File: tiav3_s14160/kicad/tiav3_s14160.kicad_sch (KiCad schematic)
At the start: 22 parts, among them J1 SSQ-103-01-G-D, J2 Conn_Coaxial, U1 OPA847IDBVT

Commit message: Tune tiav3 LPF values and export gerbers
Update LPF component values (560nH->330nH, 120pF->62pF) and tighten via diameter/drill DRC. Redirect plot/step outputs to ../manufacturing/ and commit the generated gerber set.
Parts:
- C2: value 120pF -> 62pF
- C3: value 120p -> 62pF
- L2: value 560nH -> 330nH
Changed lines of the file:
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@@
 			)
 		)
-		(property "Value" "560nH"
+		(property "Value" "330nH"
 			(at 233.553 109.271 0)
 			(effects
@@
 			)
 		)
-		(property "Value" "120pF"
+		(property "Value" "62pF"
 			(at 225.425 120.015 0)
 			(effects
@@
 			)
 		)
-		(property "Value" "120p"
+		(property "Value" "62pF"
 			(at 240.665 120.015 0)
 			(effects

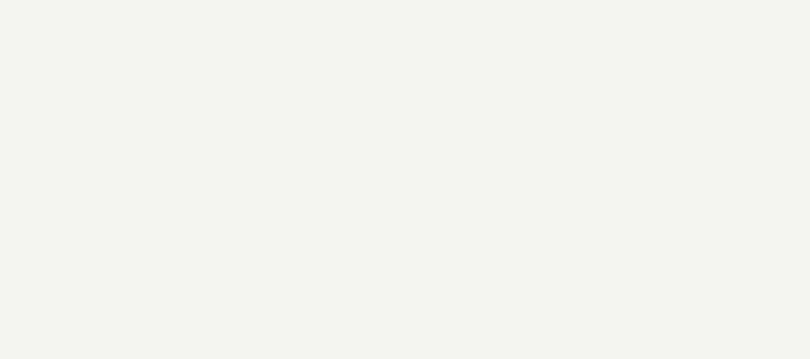
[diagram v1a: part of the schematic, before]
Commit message: Update KiCad designs for all 3 boards and re-export gerbers
- bias-control-lt8362: schematic + PCB updates, exported gerbers
  including new B_Paste/F_Paste layers
- power-supply: schematic + PCB updates, re-exported gerbers with new
  naming (.gbl/.gbs/.gto/.gtl/.gts) replacing old .gbr files, added
  paste layer exports
- tiav3_s14160: schematic + PCB updates, re-exported gerbers with new
  naming, added paste layer exports
- fp-lib-table updates across all four board projects
- new "w paste" gerber zip exports for assembly
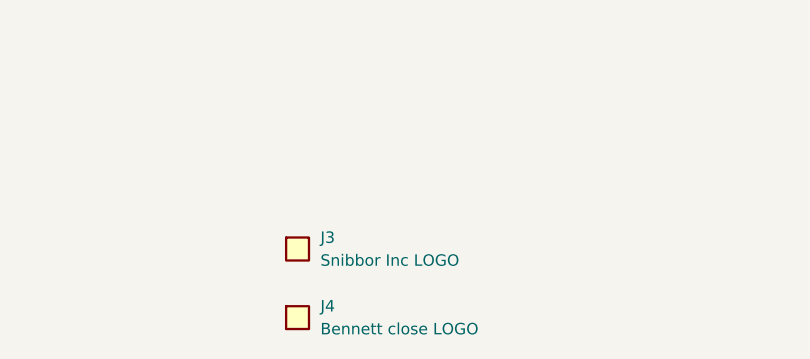
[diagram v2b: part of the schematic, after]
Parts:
- added J3: Snibbor Inc LOGO, snibbor_logos:snibbor_inc_logo, symbol Connector_Generic:Conn_01x01
- added J4: Bennett close LOGO, snibbor_logos:Bennett logo close 1 layered, symbol Connector_Generic:Conn_01x01
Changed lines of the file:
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@@
+	)
+	(symbol
+		(lib_id "Connector_Generic:Conn_01x01")
+		(at 49.53 172.72 0)
+		(unit 1)
+		(exclude_from_sim no)
+		(in_bom yes)
+		(on_board yes)
+		(dnp no)
+		(fields_autoplaced yes)
+		(property "Reference" "J4"
+			(at 52.07 171.4499 0)
+			(effects
+				(font
+					(size 1.27 1.27)
+				)
+				(justify left)
+			)
+		)
+		(property "Value" "Bennett close LOGO"
+			(at 52.07 173.9899 0)
+			(effects
+				(font
+					(size 1.27 1.27)
+				)
+				(justify left)
+			)
+		)
+		(property "Footprint" "snibbor_logos:Bennett logo close 1 layered"
+			(at 49.53 172.72 0)
+			(effects
+				(font
+					(size 1.27 1.27)
+				)
+				(hide yes)
+			)
+		)
+		(property "Datasheet" ""
+			(at 49.53 172.72 0)
+			(effects
+				(font
+					(size 1.27 1.27)
+				)
+				(hide yes)
+			)
+		)
+		(property "Description" ""
+			(at 49.53 172.72 0)
+			(effects
+				(font
+					(size 1.27 1.27)
+				)
+				(hide yes)
+			)
+		)
+		(instances
+			(project "tiav3_s14160"
+				(path "/548ba79d-aa60-452e-83bc-59e3672545ef"
+					(reference "J4")
+					(unit 1)
+				)
+			)
+		)
 	)
 	(symbol
@@
 					(unit 1)
 				)
+			)
+		)
+	)
+	(symbol
+		(lib_id "Connector_Generic:Conn_01x01")
+		(at 49.53 165.1 0)
+		(unit 1)
+		(exclude_from_sim no)
+		(in_bom yes)
+		(on_board yes)
+		(dnp no)
+		(fields_autoplaced yes)
+		(property "Reference" "J3"
+			(at 52.07 163.8299 0)
+			(effects
+				(font
+					(size 1.27 1.27)
+				)
+				(justify left)
+			)
+		)
+		(property "Value" "Snibbor Inc LOGO"
+			(at 52.07 166.3699 0)
+			(effects
+				(font
+					(size 1.27 1.27)
+				)
+				(justify left)
+			)
+		)
+		(property "Footprint" "snibbor_logos:snibbor_inc_logo"
+			(at 49.53 165.1 0)
+			(effects
+				(font
+					(size 1.27 1.27)
+				)
+				(hide yes)
+			)
+		)
+		(property "Datasheet" ""
+			(at 49.53 165.1 0)
+			(effects
+				(font
+					(size 1.27 1.27)
+				)
+				(hide yes)
+			)
+		)
+		(property "Description" ""
+			(at 49.53 165.1 0)
+			(effects
+				(font
+					(size 1.27 1.27)
+				)
+				(hide yes)
+			)
+		)
+		(instances
+			(project ""
+				(path "/548ba79d-aa60-452e-83bc-59e3672545ef"
+					(reference "J3")
+					(unit 1)
+				)
